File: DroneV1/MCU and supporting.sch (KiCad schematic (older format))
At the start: 7 parts, among them U1 ESP8266EX, Y1 Crystal_GND24

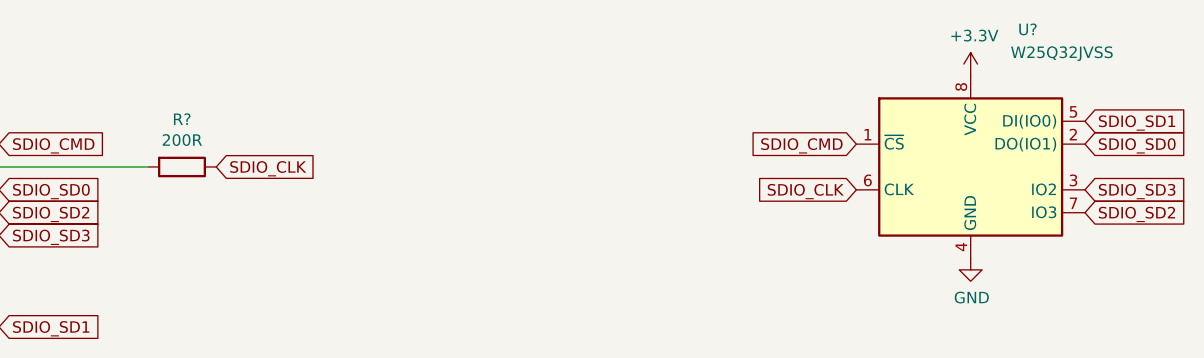
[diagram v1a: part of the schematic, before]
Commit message: Added indicator LEDs
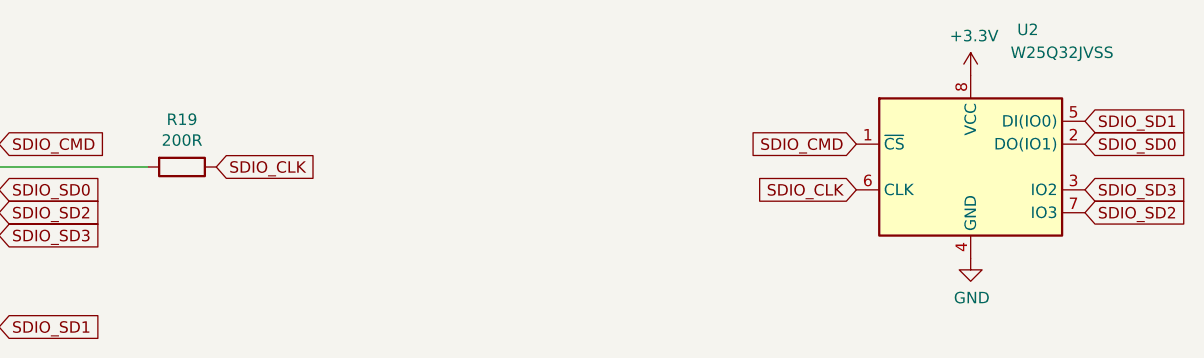
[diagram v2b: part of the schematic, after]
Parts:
- C2, C3: footprint (none) -> Capacitor_SMD:C_0603_1608Metric
- R19: renamed from R?; footprint (none) -> Resistor_SMD:R_0603_1608Metric
- RN1: footprint (none) -> Package_DIP:DIP-8-16_W7.62mm
- gave numbers to parts that had none: 1
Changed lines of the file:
@@
 F 0 "RN1" V 3933 3100 50  0000 C CNN
 F 1 "R_Pack04" V 4024 3100 50  0000 C CNN
-F 2 "" V 4625 3100 50  0001 C CNN
+F 2 "Package_DIP:DIP-8-16_W7.62mm" V 4625 3100 50  0001 C CNN
 F 3 "~" H 4350 3100 50  0001 C CNN
 	1    4350 3100
@@
 F 0 "C3" H 1450 3350 50  0000 L CNN
 F 1 "C" H 1450 3150 50  0000 L CNN
-F 2 "" H 1438 3100 50  0001 C CNN
+F 2 "Capacitor_SMD:C_0603_1608Metric" H 1438 3100 50  0001 C CNN
 F 3 "~" H 1400 3250 50  0001 C CNN
 	1    1400 3250
@@
 F 0 "C2" H 1515 2696 50  0000 L CNN
 F 1 "C" H 1515 2605 50  0000 L CNN
-F 2 "" H 1438 2500 50  0001 C CNN
+F 2 "Capacitor_SMD:C_0603_1608Metric" H 1438 2500 50  0001 C CNN
 F 3 "~" H 1400 2650 50  0001 C CNN
 	1    1400 2650
@@
 Connection ~ 1400 3100
 $Comp
-L power:GND #PWR?
+L power:GND #PWR043
 U 1 1 5E04EC21
 P 2850 3500
-F 0 "#PWR?" H 2850 3250 50  0001 C CNN
+F 0 "#PWR043" H 2850 3250 50  0001 C CNN
 F 1 "GND" H 2855 3327 50  0000 C CNN
 F 2 "" H 2850 3500 50  0001 C CNN
@@
 $EndComp
 $Comp
-L Memory_Flash:W25Q32JVSS U?
+L Memory_Flash:W25Q32JVSS U2
 U 1 1 5E052876
 P 8000 1800
-F 0 "U?" H 8250 2400 50  0000 C CNN
+F 0 "U2" H 8250 2400 50  0000 C CNN
 F 1 "W25Q32JVSS" H 8400 2300 50  0000 C CNN
 F 2 "Package_SO:SOIC-8_5.23x5.23mm_P1.27mm" H 8000 1800 50  0001 C CNN
@@
 $EndComp
 $Comp
-L power:GND #PWR?
+L power:GND #PWR045
 U 1 1 5E053250
 P 8000 2200
-F 0 "#PWR?" H 8000 1950 50  0001 C CNN
+F 0 "#PWR045" H 8000 1950 50  0001 C CNN
 F 1 "GND" H 8005 2027 50  0000 C CNN
 F 2 "" H 8000 2200 50  0001 C CNN
@@
 $EndComp
 $Comp
-L power:+3.3V #PWR?
+L power:+3.3V #PWR044
 U 1 1 5E0536C8
 P 8000 1400
-F 0 "#PWR?" H 8000 1250 50  0001 C CNN
+F 0 "#PWR044" H 8000 1250 50  0001 C CNN
 F 1 "+3.3V" H 8015 1573 50  0000 C CNN
 F 2 "" H 8000 1400 50  0001 C CNN
@@
 SDIO_SD1
 $Comp
-L Device:R R?
+L Device:R R19
 U 1 1 5E0554BD
 P 4550 1800
-F 0 "R?" V 4343 1800 50  0000 C CNN
+F 0 "R19" V 4343 1800 50  0000 C CNN
 F 1 "200R" V 4434 1800 50  0000 C CNN
-F 2 "" V 4480 1800 50  0001 C CNN
+F 2 "Resistor_SMD:R_0603_1608Metric" V 4480 1800 50  0001 C CNN
 F 3 "~" H 4550 1800 50  0001 C CNN
 	1    4550 1800
